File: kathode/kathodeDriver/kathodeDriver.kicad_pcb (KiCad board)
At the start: 2 copper layers, 162.5 x 13.2 mm, 159 parts, among them J1 Conn_01x04, J2 Conn_01x02, U1 74AUP1G32, U10 4017, U11 4017, U2 4017, U3 4081, U4 4081, U5 4017, U6 4017, U7 4017, U8 4017, U9 4017

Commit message: Started work on layout
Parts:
- added Q1: Q_NPN_BEC, Package_TO_SOT_SMD:SOT-23, F.Cu at (84.2, 72.0)
- added Q10: Q_NPN_BEC, Package_TO_SOT_SMD:SOT-23, F.Cu at (104.0, 72.0)
- added Q11: Q_NPN_BEC, Package_TO_SOT_SMD:SOT-23, F.Cu at (120.0, 72.1)
- added Q12: Q_NPN_BEC, Package_TO_SOT_SMD:SOT-23, F.Cu at (135.0, 63.0)
- added Q13: Q_NPN_BEC, Package_TO_SOT_SMD:SOT-23, F.Cu at (194.2, 40.2)
- added Q14: Q_NPN_BEC, Package_TO_SOT_SMD:SOT-23, F.Cu at (198.8, 40.2)
- added Q15: Q_NPN_BEC, Package_TO_SOT_SMD:SOT-23, F.Cu at (203.4, 40.2)
- added Q16: Q_NPN_BEC, Package_TO_SOT_SMD:SOT-23, F.Cu at (216.0, 61.0)
- added Q17: Q_NPN_BEC, Package_TO_SOT_SMD:SOT-23, F.Cu at (91.2, 63.0)
- added Q18: Q_NPN_BEC, Package_TO_SOT_SMD:SOT-23, F.Cu at (107.0, 63.0)
- added Q19: Q_NPN_BEC, Package_TO_SOT_SMD:SOT-23, F.Cu at (123.0, 63.1)
- added Q2: Q_NPN_BEC, Package_TO_SOT_SMD:SOT-23, F.Cu at (103.0, 63.0)
- added Q20: Q_NPN_BEC, Package_TO_SOT_SMD:SOT-23, F.Cu at (143.0, 68.0)
- added Q21: Q_NPN_BEC, Package_TO_SOT_SMD:SOT-23, F.Cu at (194.2, 35.3)
- added Q22: Q_NPN_BEC, Package_TO_SOT_SMD:SOT-23, F.Cu at (198.8, 35.3)
- added Q23: Q_NPN_BEC, Package_TO_SOT_SMD:SOT-23, F.Cu at (203.4, 35.3)
- added Q24: Q_NPN_BEC, Package_TO_SOT_SMD:SOT-23, F.Cu at (208.1, 35.3)
- added Q25: Q_NPN_BEC, Package_TO_SOT_SMD:SOT-23, F.Cu at (92.0, 72.1)
- added Q26: Q_NPN_BEC, Package_TO_SOT_SMD:SOT-23, F.Cu at (108.0, 72.1)
- added Q27: Q_NPN_BEC, Package_TO_SOT_SMD:SOT-23, F.Cu at (124.0, 72.0)
- added Q28: Q_NPN_BEC, Package_TO_SOT_SMD:SOT-23, F.Cu at (150.9, 62.1)
- added Q29: Q_NPN_BEC, Package_TO_SOT_SMD:SOT-23, F.Cu at (194.2, 30.4)
- added Q3: Q_NPN_BEC, Package_TO_SOT_SMD:SOT-23, F.Cu at (119.0, 63.1)
- added Q30: Q_NPN_BEC, Package_TO_SOT_SMD:SOT-23, F.Cu at (198.8, 30.4)
- added Q31: Q_NPN_BEC, Package_TO_SOT_SMD:SOT-23, F.Cu at (203.4, 30.4)
- added Q32: Q_NPN_BEC, Package_TO_SOT_SMD:SOT-23, F.Cu at (208.0, 62.9)
- added Q33: Q_NPN_BEC, Package_TO_SOT_SMD:SOT-23, F.Cu at (95.0, 63.0)
- added Q34: Q_NPN_BEC, Package_TO_SOT_SMD:SOT-23, F.Cu at (111.0, 63.0)
- added Q35: Q_NPN_BEC, Package_TO_SOT_SMD:SOT-23, F.Cu at (127.0, 63.1)
- added Q36: Q_NPN_BEC, Package_TO_SOT_SMD:SOT-23, F.Cu at (151.0, 70.9)
- added Q37: Q_NPN_BEC, Package_TO_SOT_SMD:SOT-23, F.Cu at (194.2, 25.5)
- added Q38: Q_NPN_BEC, Package_TO_SOT_SMD:SOT-23, F.Cu at (198.8, 25.5)
- added Q39: Q_NPN_BEC, Package_TO_SOT_SMD:SOT-23, F.Cu at (201.0, 65.9)
- added Q4: Q_NPN_BEC, Package_TO_SOT_SMD:SOT-23, F.Cu at (136.0, 72.0)
- added Q40: Q_NPN_BEC, Package_TO_SOT_SMD:SOT-23, F.Cu at (208.1, 25.5)
- added Q41: Q_NPN_BEC, Package_TO_SOT_SMD:SOT-23, F.Cu at (96.0, 72.0)
- added Q42: Q_NPN_BEC, Package_TO_SOT_SMD:SOT-23, F.Cu at (112.0, 72.1)
- added Q43: Q_NPN_BEC, Package_TO_SOT_SMD:SOT-23, F.Cu at (128.0, 72.0)
- added Q44: Q_NPN_BEC, Package_TO_SOT_SMD:SOT-23, F.Cu at (147.1, 63.1)
- added Q45: Q_NPN_BEC, Package_TO_SOT_SMD:SOT-23, F.Cu at (194.2, 20.6)
- added Q46: Q_NPN_BEC, Package_TO_SOT_SMD:SOT-23, F.Cu at (198.8, 20.6)
- added Q47: Q_NPN_BEC, Package_TO_SOT_SMD:SOT-23, F.Cu at (203.4, 20.6)
- added Q48: Q_NPN_BEC, Package_TO_SOT_SMD:SOT-23, F.Cu at (208.1, 20.6)
- added Q49: Q_NPN_BEC, Package_TO_SOT_SMD:SOT-23, F.Cu at (99.0, 63.0)
- added Q5: Q_NPN_BEC, Package_TO_SOT_SMD:SOT-23, F.Cu at (194.2, 45.1)
- added Q50: Q_NPN_BEC, Package_TO_SOT_SMD:SOT-23, F.Cu at (115.0, 63.0)
- added Q51: Q_NPN_BEC, Package_TO_SOT_SMD:SOT-23, F.Cu at (131.1, 63.1)
- added Q52: Q_NPN_BEC, Package_TO_SOT_SMD:SOT-23, F.Cu at (151.1, 65.1)
- added Q53: Q_NPN_BEC, Package_TO_SOT_SMD:SOT-23, F.Cu at (194.2, 15.7)
- added Q54: Q_NPN_BEC, Package_TO_SOT_SMD:SOT-23, F.Cu at (198.8, 15.7)
- added Q55: Q_NPN_BEC, Package_TO_SOT_SMD:SOT-23, F.Cu at (203.4, 15.7)
- added Q56: Q_NPN_BEC, Package_TO_SOT_SMD:SOT-23, F.Cu at (193.9, 62.1)
- added Q57: Q_NPN_BEC, Package_TO_SOT_SMD:SOT-23, F.Cu at (100.0, 72.0)
- added Q58: Q_NPN_BEC, Package_TO_SOT_SMD:SOT-23, F.Cu at (116.0, 72.1)
- added Q59: Q_NPN_BEC, Package_TO_SOT_SMD:SOT-23, F.Cu at (131.9, 72.1)
- added Q6: Q_NPN_BEC, Package_TO_SOT_SMD:SOT-23, F.Cu at (198.8, 45.1)
- added Q60: Q_NPN_BEC, Package_TO_SOT_SMD:SOT-23, F.Cu at (156.0, 64.0)
- added Q61: Q_NPN_BEC, Package_TO_SOT_SMD:SOT-23, F.Cu at (194.2, 10.8)
- added Q62: Q_NPN_BEC, Package_TO_SOT_SMD:SOT-23, F.Cu at (198.8, 10.8)
- added Q63: Q_NPN_BEC, Package_TO_SOT_SMD:SOT-23, F.Cu at (220.0, 68.9)
- added Q64: Q_NPN_BEC, Package_TO_SOT_SMD:SOT-23, F.Cu at (221.0, 62.0)
- added Q7: Q_NPN_BEC, Package_TO_SOT_SMD:SOT-23, F.Cu at (203.4, 45.1)
- added Q8: Q_NPN_BEC, Package_TO_SOT_SMD:SOT-23, F.Cu at (208.1, 45.1)
- added Q9: Q_NPN_BEC, Package_TO_SOT_SMD:SOT-23, F.Cu at (88.2, 72.0)
- moved R113 100.0 mm to (203.5, 17.0), turned to 90 degrees
- moved R112 97.0 mm to (199.5, 16.0), turned to 90 degrees
- moved R111 92.5 mm to (195.0, 16.5), turned to 90 degrees
- moved R128 92.0 mm to (199.5, 11.1), turned to 90 degrees
- moved R75 86.8 mm to (95.0, 60.0), turned to 180 degrees
- moved R82 84.1 mm to (208.0, 26.1), turned to 90 degrees
- moved R107 81.8 mm to (99.0, 60.0), turned to 180 degrees
- moved R91 80.4 mm to (96.0, 69.0), turned to 180 degrees
- moved R123 79.3 mm to (100.0, 69.0), turned to 180 degrees
- moved R43 78.3 mm to (91.2, 60.0)
- moved R98 77.9 mm to (208.0, 21.9), turned to 90 degrees
- moved R18 77.4 mm to (208.0, 46.5), turned to 90 degrees
- moved R27 77.0 mm to (88.1, 69.0), turned to 180 degrees
- moved R34 76.0 mm to (220.0, 48.0), turned to 90 degrees
- moved R59 74.8 mm to (92.0, 69.1), turned to 180 degrees
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
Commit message: Lots of routing done
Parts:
- moved R122 84.8 mm to (225.2, 66.0)
- moved R74 81.2 mm to (215.2, 74.9)
- moved R90 81.2 mm to (220.9, 66.0)
- moved R58 78.5 mm to (217.1, 66.0)
- moved R42 78.0 mm to (211.2, 74.9)
- moved R26 76.3 mm to (213.1, 66.0)
- moved R10 75.6 mm to (207.3, 74.9)
- moved R73 72.8 mm to (201.2, 66.0)
- moved C2 69.9 mm to (198.2, 105.0)
- moved R121 69.8 mm to (209.1, 66.0)
- moved R106 69.1 mm to (219.2, 74.9)
- moved R41 68.5 mm to (197.2, 66.0)
- moved R89 65.9 mm to (205.1, 66.0)
- moved R9 64.8 mm to (193.2, 66.0)
- moved Q61 64.2 mm to (174.9, 72.1)
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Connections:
- Q62 pad 3: /OUT_K48 -> /OUT_K47
- R128 pad 2: /OUT_K48 -> /OUT_K47
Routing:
- net HT: track 0.00 -> 67.8 mm, vias 0 -> 63
- net /OUT_K1: track 0.00 -> 24.1 mm, vias 0 -> 1
- net /OUT_K3: track 0.00 -> 23.8 mm, vias 0 -> 1
- net /OUT_K0: track 0.00 -> 23.7 mm, vias 0 -> 1
- net /OUT_K60: track 0.00 -> 23.4 mm, vias 0 -> 1
- net /OUT_K5: track 0.00 -> 23.0 mm, vias 0 -> 1
- net /OUT_K58: track 0.00 -> 22.9 mm, vias 0 -> 1
- net /OUT_K62: track 0.00 -> 22.7 mm, vias 0 -> 1
- net /OUT_K7: track 0.00 -> 22.4 mm, vias 0 -> 1
- net /OUT_K29: track 0.00 -> 21.8 mm, vias 0 -> 1
- net /OUT_K9: track 0.00 -> 21.7 mm, vias 0 -> 1
- net /OUT_K11: track 0.00 -> 21.3 mm, vias 0 -> 1
- net /OUT_K31: track 0.00 -> 21.2 mm, vias 0 -> 1
- net /OUT_K56: track 0.00 -> 21.0 mm, vias 0 -> 1
- net /OUT_K54: track 0.00 -> 20.8 mm, vias 0 -> 1
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- added copper zone on In1.Cu, net HT
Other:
- copper layers 2 -> 4

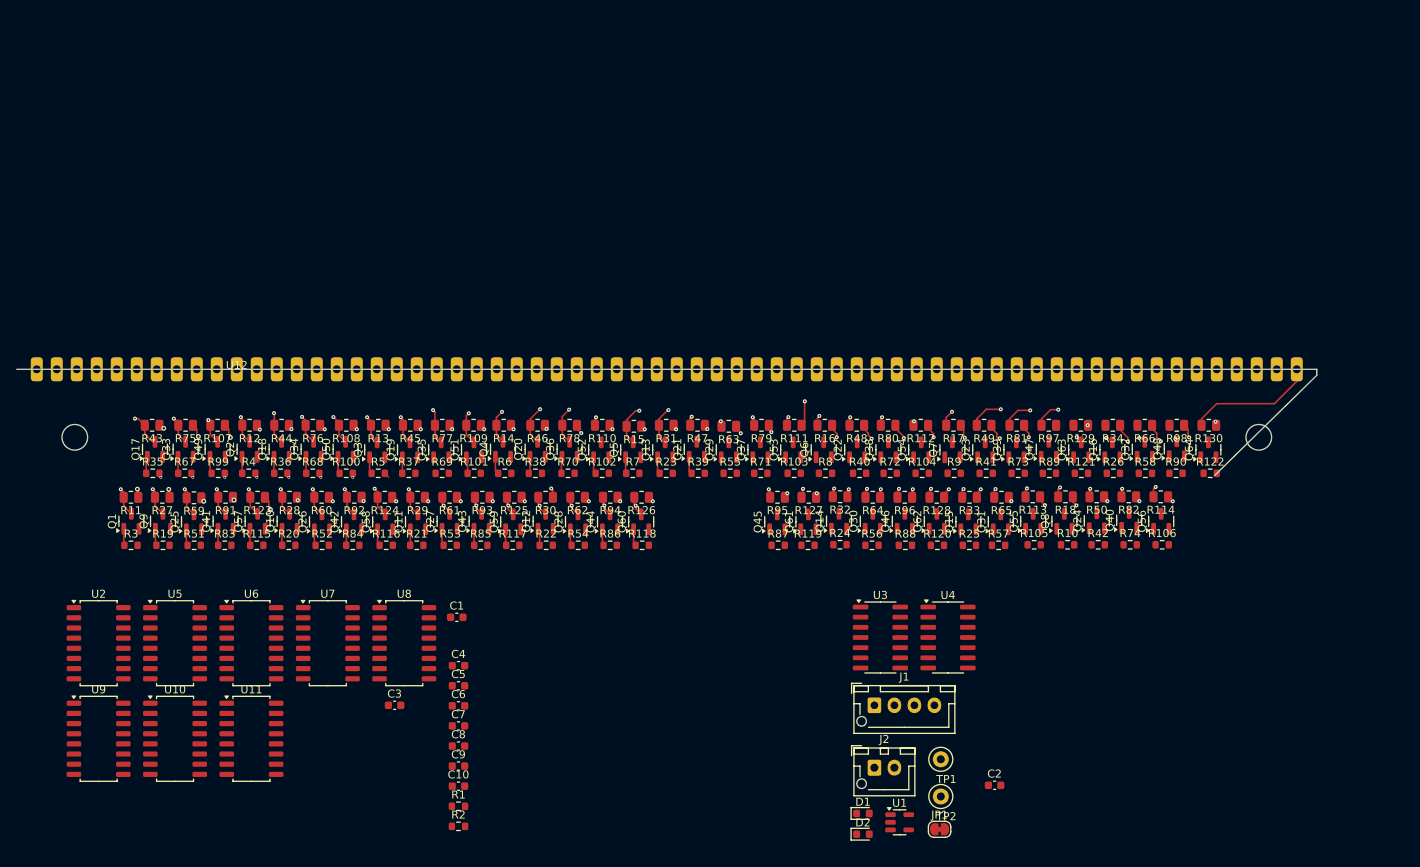
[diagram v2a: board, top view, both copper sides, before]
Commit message: Finished the kathode driver, onto the anodes
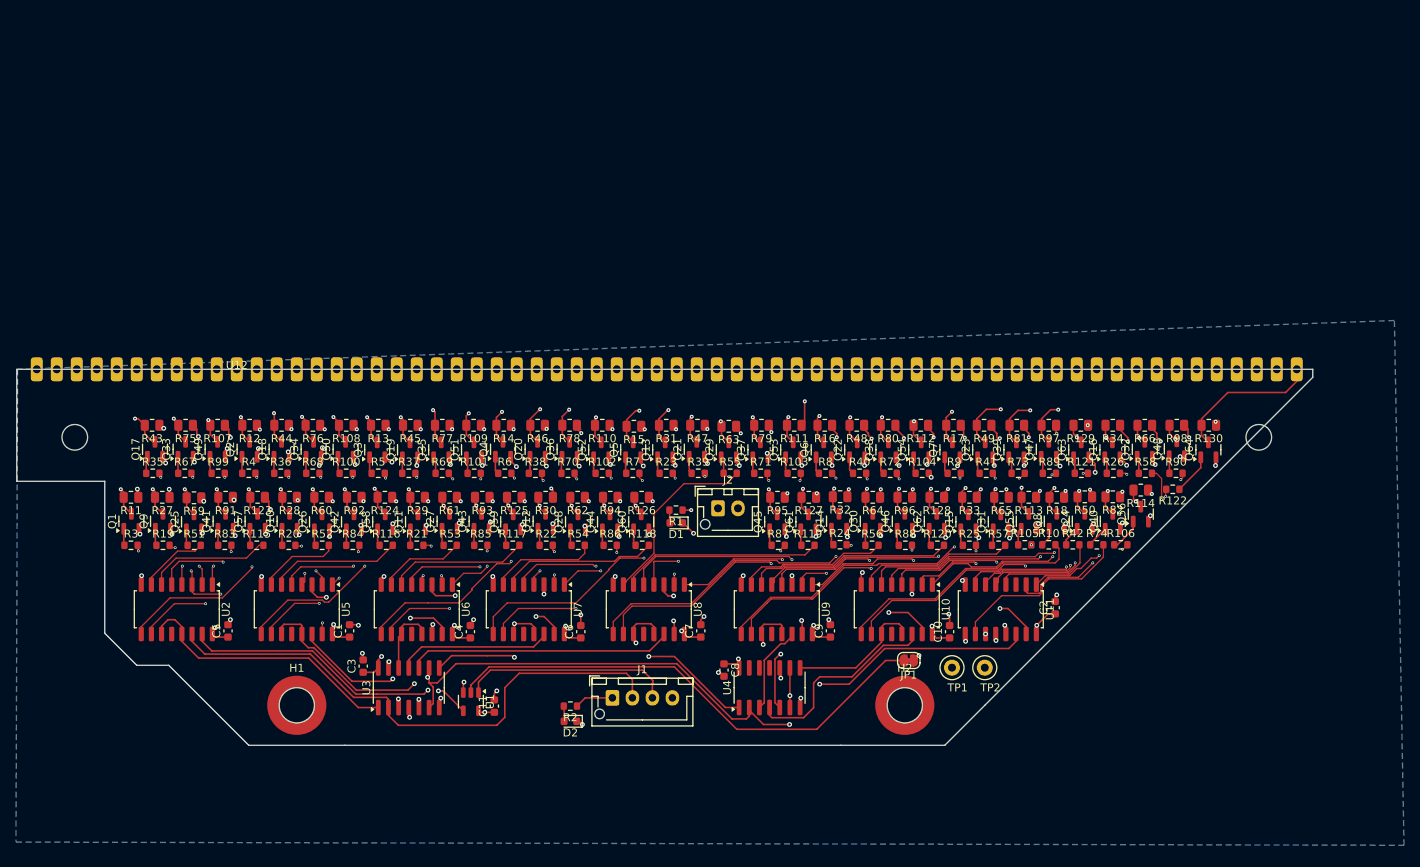
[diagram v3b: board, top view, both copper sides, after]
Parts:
- added C11: 1uF, Capacitor_SMD:C_0603_1608Metric, F.Cu at (135.7, 95.1)
- added H1: MountingHole, Mounting_Wuerth:Mounting_Wuerth_WA-SMSI-M3_H2mm_9774020360, F.Cu at (111.0, 95.0)
- added H2: MountingHole, Mounting_Wuerth:Mounting_Wuerth_WA-SMSI-M3_H2mm_9774020360, F.Cu at (187.0, 95.0)
- moved U11 95.1 mm to (199.0, 83.0), turned to -90 degrees
- moved U10 91.7 mm to (186.0, 83.0), turned to -90 degrees
- moved U9 86.3 mm to (171.0, 83.0), turned to -90 degrees
- moved C10 64.4 mm to (192.6, 85.8), turned to 90 degrees
- moved U3 59.3 mm to (125.0, 92.8), turned to 90 degrees
- moved U1 55.7 mm to (132.8, 94.5), turned to -90 degrees
- moved C9 49.5 mm to (177.7, 85.7), turned to 90 degrees
- moved R1 45.9 mm to (158.4, 70.6), turned to 180 degrees
- moved D1 43.2 mm to (158.4, 72.2), turned to 180 degrees
- moved D2 39.2 mm to (145.2, 97.0), turned to 180 degrees
- moved J2 37.9 mm to (163.7, 70.4)
- moved C8 34.5 mm to (164.4, 90.6), turned to -90 degrees
- moved J1 32.8 mm to (150.4, 94.1)
- moved C7 32.5 mm to (161.5, 85.7), turned to 90 degrees
- moved U8 30.9 mm to (155.0, 83.0), turned to -90 degrees
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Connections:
- R104 pad 2: /uK46 -> /K46
- U3 pad 10: Net-(U7-CLK) -> Net-(U8-CLK)
- U3 pad 11: Net-(U8-CLK) -> Net-(U7-CLK)
- U3 pad 12: Net-(U7-CKEN) -> Net-(U6-CKEN)
- U3 pad 13: unconnected-(U3-Pad13) -> /CLK
- U3 pad 8: Net-(U6-CKEN) -> Net-(U7-CKEN)
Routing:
- net VCC: track 0.00 -> 175.4 mm, vias 0 -> 11
- net GND: track 0.00 -> 92.7 mm, vias 0 -> 90
- net /CLK: track 0.00 -> 71.6 mm, vias 0 -> 4
- net /INPUT_CLK: track 0.00 -> 69.0 mm
- net /LAST_COUNT_RESET: track 0.00 -> 62.8 mm
- net /K40: track 0.00 -> 44.1 mm, vias 0 -> 2
- net /K48: track 0.00 -> 41.2 mm, vias 0 -> 2
- net Net-(U2-Reset): track 0.00 -> 37.6 mm, vias 0 -> 2
- net /K52: track 0.00 -> 36.8 mm, vias 0 -> 2
- net /K55: track 0.00 -> 36.6 mm, vias 0 -> 2
- net /K36: track 0.00 -> 36.1 mm, vias 0 -> 2
- net /K32: track 0.00 -> 34.9 mm, vias 0 -> 2
- net Net-(U11-CLK): track 0.00 -> 34.2 mm, vias 0 -> 2
- net Net-(U2-CKEN): track 0.00 -> 34.0 mm
- net /K44: track 0.00 -> 33.7 mm, vias 0 -> 2
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- added copper zone on B.Cu, net GND
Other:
- board size 162.5 x 13.2 mm -> 162 x 47 mm

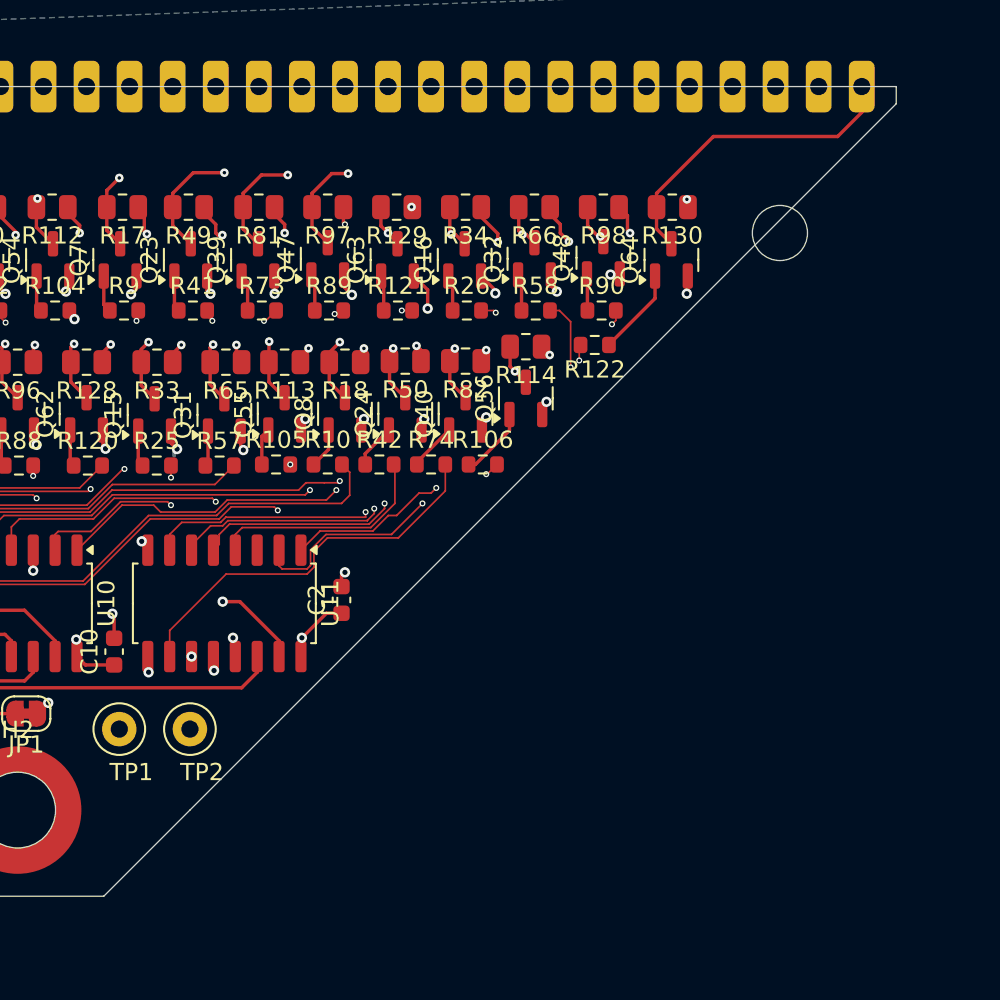
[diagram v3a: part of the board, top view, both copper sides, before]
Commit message: Added design files for the kathode, mods to the anode board
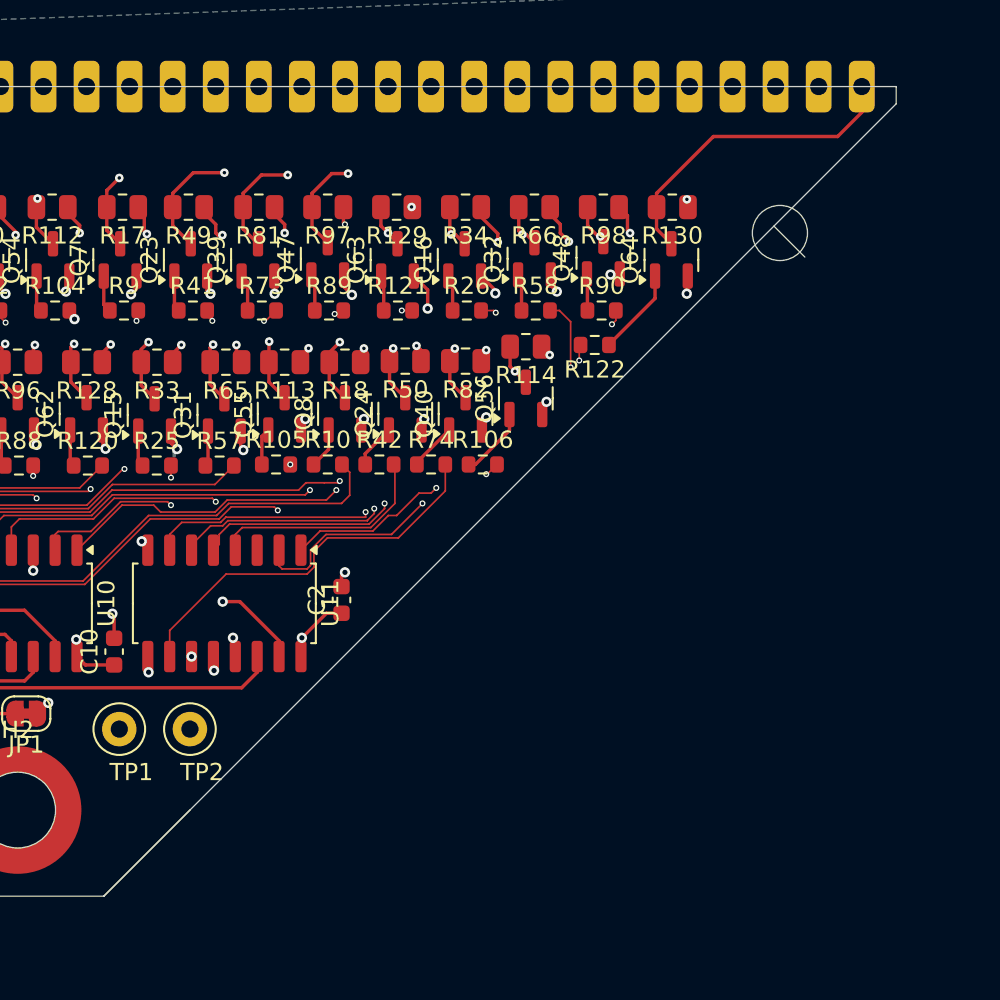
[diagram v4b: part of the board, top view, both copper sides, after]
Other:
- outline, holes or cut-outs redrawn
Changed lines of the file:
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@@
 	)
 	(gr_line
-		(start 238 54)
-		(end 197 95)
+		(start 230.9 61.1)
+		(end 232.7 62.9)
 		(stroke
 			(width 0.05)
@@
 	)
 	(gr_line
+		(start 238 54)
+		(end 192 100)
+		(stroke
+			(width 0.05)
+			(type default)
+		)
+		(layer "Edge.Cuts")
+	)
+	(gr_line
 		(start 95 90)
 		(end 91 90)
@@
 		(layer "Edge.Cuts")
 	)
+	(dimension
+		(type aligned)
+		(layer "Edge.Cuts")
+		(pts
+			(xy 187 95) (xy 187 100.1)
+		)
+		(height -3.1)
+		(gr_text "5.1000 mm"
+			(at 188.95 97.55 90)
+			(layer "Edge.Cuts")
+			(effects
+				(font
+					(size 1 1)
+					(thickness 0.15)
+				)
+			)
+		)
+		(format
+			(prefix "")
+			(suffix "")
+			(units 3)
+			(units_format 1)
+			(precision 4)
+		)
+		(style
+			(thickness 0.05)
+			(arrow_length 1.27)
+			(text_position_mode 0)
+			(extension_height 0.58642)
+			(extension_offset 0.5) keep_text_aligned)
+	)
+	(dimension
+		(type aligned)
+		(layer "Edge.Cuts")
+		(pts
+			(xy 187 95) (xy 111 95)
+		)
+		(height -11.9)
+		(gr_text "76.0000 mm"
+			(at 149 105.75 0)
+			(layer "Edge.Cuts")
+			(effects
+				(font
+					(size 1 1)
+					(thickness 0.15)
+				)
+			)
+		)
+		(format
+			(prefix "")
+			(suffix "")
+			(units 3)
+			(units_format 1)
+			(precision 4)
+		)
+		(style
+			(thickness 0.05)
+			(arrow_length 1.27)
+			(text_position_mode 0)
+			(extension_height 0.58642)
+			(extension_offset 0.5) keep_text_aligned)
+	)
 	(segment
